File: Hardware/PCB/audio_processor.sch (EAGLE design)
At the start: 33 parts, among them IC1 ADS7042DCU, IC2 ADS7042DCU, J1 TMS-101-51-G-D, J10 TMS-101-51-G-D, J11 MTMM-101-X-X-S-X, J12 TMS-101-51-G-D, J2 MTMM-101-X-X-S-X, J3 TMS-101-51-G-D, J4 MTMM-101-X-X-S-X, J5 MTMM-101-X-X-S-X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

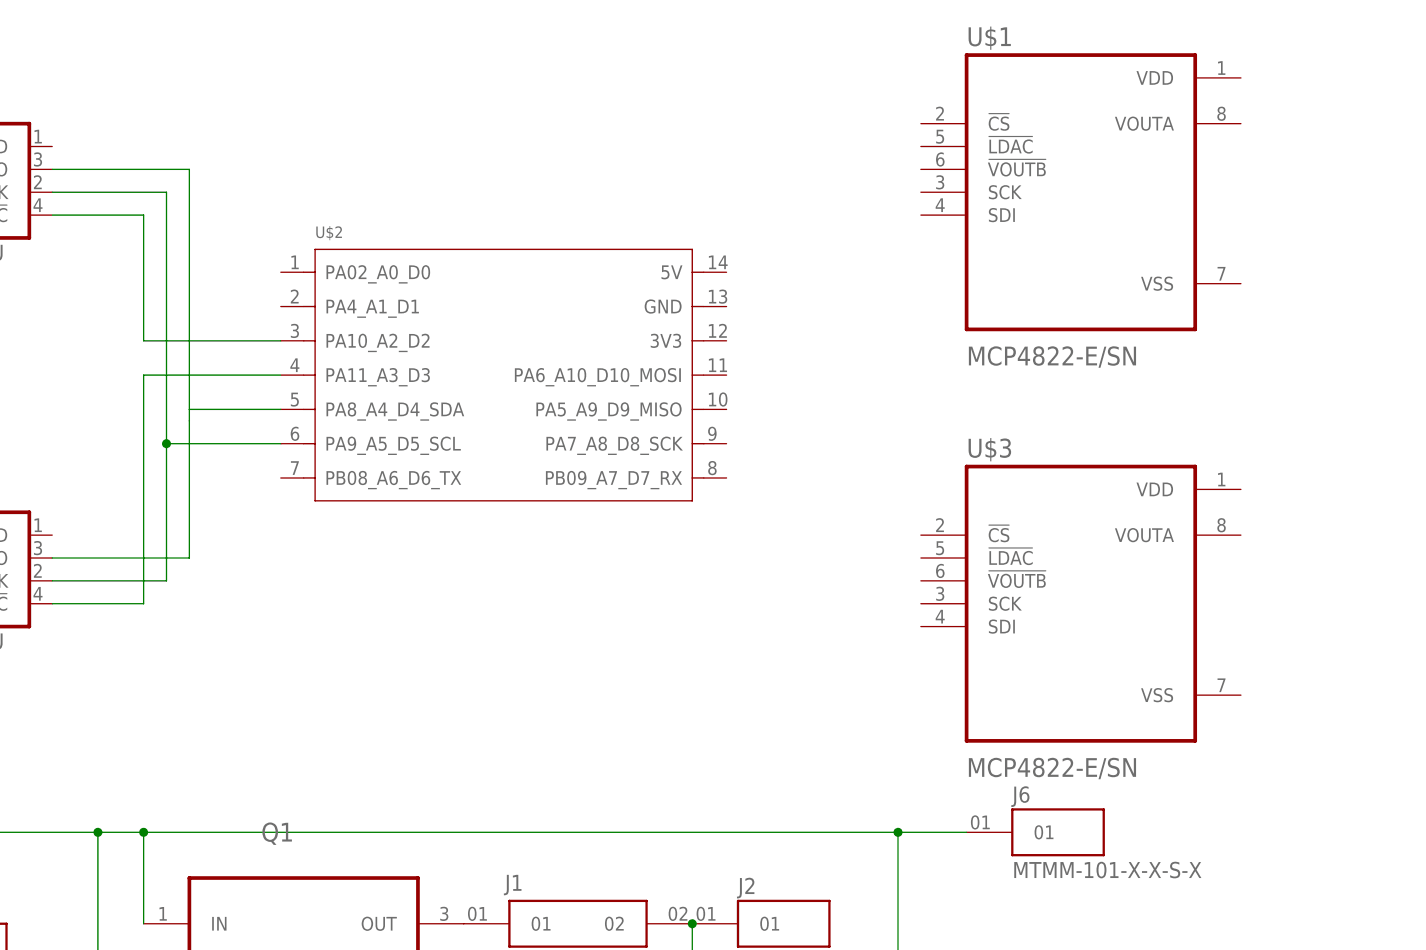
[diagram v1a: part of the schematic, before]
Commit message: AP_0_02
More README detail.
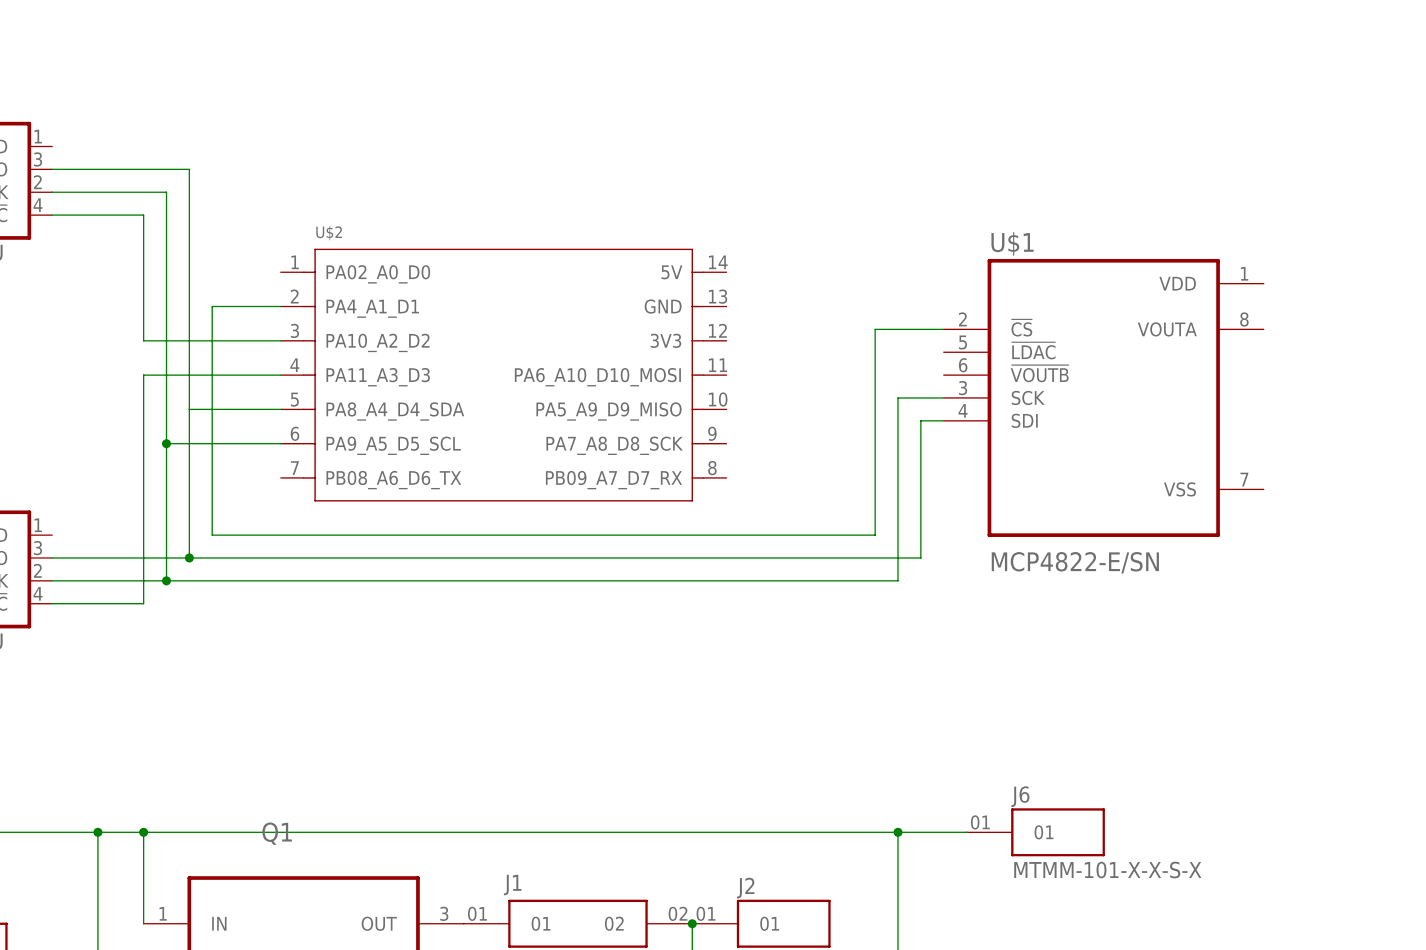
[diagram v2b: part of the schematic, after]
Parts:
- removed U$3: MCP4822-E/SN, MCP4822-E_SN:MCP4822-E/SN
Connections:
- new net N$28: U$1.!CS, U$2.PA4_A1_D1
- net N$21: now also U$1.SCK
- net N$24: now also U$1.SDI
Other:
- moved on the sheet: U$1
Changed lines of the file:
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@@
 </part>
 <part name="IC2" library="Texas Instruments" deviceset="ADS7042" device="DCU" package3d_urn="urn:adsk.eagle:package:7566972/2"/>
-<part name="U$3" library="MCP4822-E_SN" deviceset="MCP4822-E/SN" device=""/>
 </parts>
 <sheets>
@@
 <attribute name="VALUE" x="119.38" y="134.62" size="1.778" layer="96"/>
 </instance>
-<instance part="U$1" gate="A" x="254" y="185.42" smashed="yes">
-<attribute name="NAME" x="241.3" y="201.66" size="2.0828" layer="95" ratio="10" rot="SR0"/>
-<attribute name="VALUE" x="241.3" y="166.18" size="2.0828" layer="96" ratio="10" rot="SR0"/>
+<instance part="U$1" gate="A" x="256.54" y="162.56" smashed="yes">
+<attribute name="NAME" x="243.84" y="178.8" size="2.0828" layer="95" ratio="10" rot="SR0"/>
+<attribute name="VALUE" x="243.84" y="143.32" size="2.0828" layer="96" ratio="10" rot="SR0"/>
 </instance>
 <instance part="U$2" gate="G$1" x="190.5" y="165.1" smashed="yes">
@@
 <attribute name="NAME" x="119.38" y="194.31" size="1.778" layer="95"/>
 <attribute name="VALUE" x="119.38" y="177.8" size="1.778" layer="96"/>
-</instance>
-<instance part="U$3" gate="A" x="254" y="139.7" smashed="yes">
-<attribute name="NAME" x="241.3" y="155.94" size="2.0828" layer="95" ratio="10" rot="SR0"/>
-<attribute name="VALUE" x="241.3" y="120.46" size="2.0828" layer="96" ratio="10" rot="SR0"/>
 </instance>
 </instances>
@@
 <wire x1="165.1" y1="157.48" x2="152.4" y2="157.48" width="0.1524" layer="91"/>
 <junction x="152.4" y="157.48"/>
+<pinref part="U$1" gate="A" pin="SCK"/>
+<wire x1="238.76" y1="162.56" x2="233.68" y2="162.56" width="0.1524" layer="91"/>
+<wire x1="233.68" y1="162.56" x2="233.68" y2="142.24" width="0.1524" layer="91"/>
+<wire x1="233.68" y1="142.24" x2="152.4" y2="142.24" width="0.1524" layer="91"/>
+<junction x="152.4" y="142.24"/>
 </segment>
 </net>
@@
 <wire x1="154.94" y1="187.96" x2="154.94" y2="161.29" width="0.1524" layer="91"/>
 <pinref part="IC1" gate="G$1" pin="SDO"/>
-<wire x1="154.94" y1="160.02" x2="154.94" y2="144.78" width="0.1524" layer="91"/>
+<wire x1="154.94" y1="161.29" x2="154.94" y2="144.78" width="0.1524" layer="91"/>
 <wire x1="154.94" y1="144.78" x2="139.7" y2="144.78" width="0.1524" layer="91"/>
 <pinref part="U$2" gate="G$1" pin="PA8_A4_D4_SDA"/>
 <wire x1="165.1" y1="161.29" x2="154.94" y2="161.29" width="0.1524" layer="91"/>
-<wire x1="154.94" y1="161.29" x2="154.94" y2="160.02" width="0.1524" layer="91"/>
+<pinref part="U$1" gate="A" pin="SDI"/>
+<wire x1="238.76" y1="160.02" x2="236.22" y2="160.02" width="0.1524" layer="91"/>
+<wire x1="236.22" y1="160.02" x2="236.22" y2="144.78" width="0.1524" layer="91"/>
+<wire x1="236.22" y1="144.78" x2="154.94" y2="144.78" width="0.1524" layer="91"/>
+<junction x="154.94" y="144.78"/>
 </segment>
 </net>
@@
 </segment>
 </net>
+<net name="N$28" class="0">
+<segment>
+<pinref part="U$1" gate="A" pin="!CS"/>
+<wire x1="238.76" y1="170.18" x2="231.14" y2="170.18" width="0.1524" layer="91"/>
+<wire x1="231.14" y1="170.18" x2="231.14" y2="147.32" width="0.1524" layer="91"/>
+<wire x1="231.14" y1="147.32" x2="157.48" y2="147.32" width="0.1524" layer="91"/>
+<wire x1="157.48" y1="147.32" x2="157.48" y2="172.72" width="0.1524" layer="91"/>
+<pinref part="U$2" gate="G$1" pin="PA4_A1_D1"/>
+<wire x1="157.48" y1="172.72" x2="165.1" y2="172.72" width="0.1524" layer="91"/>
+</segment>
+</net>

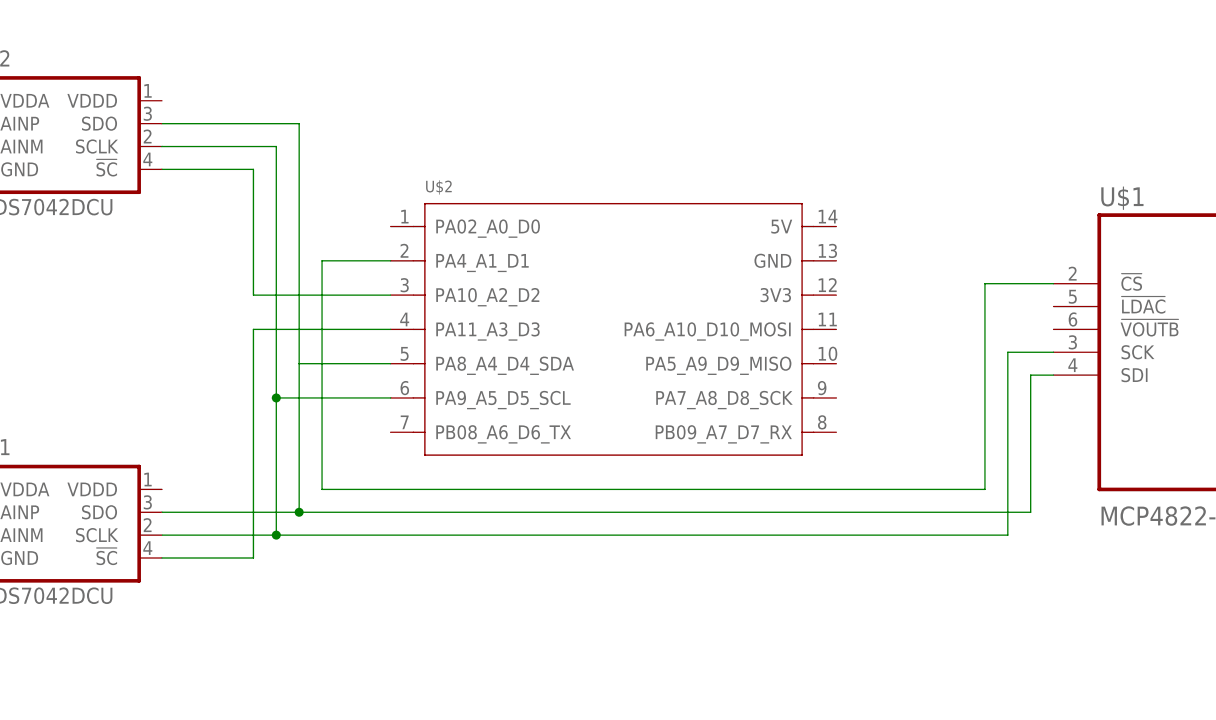
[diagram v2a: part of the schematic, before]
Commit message: AP_0_03
First public commit.  Uses timer group (as opposed to GPTimer).
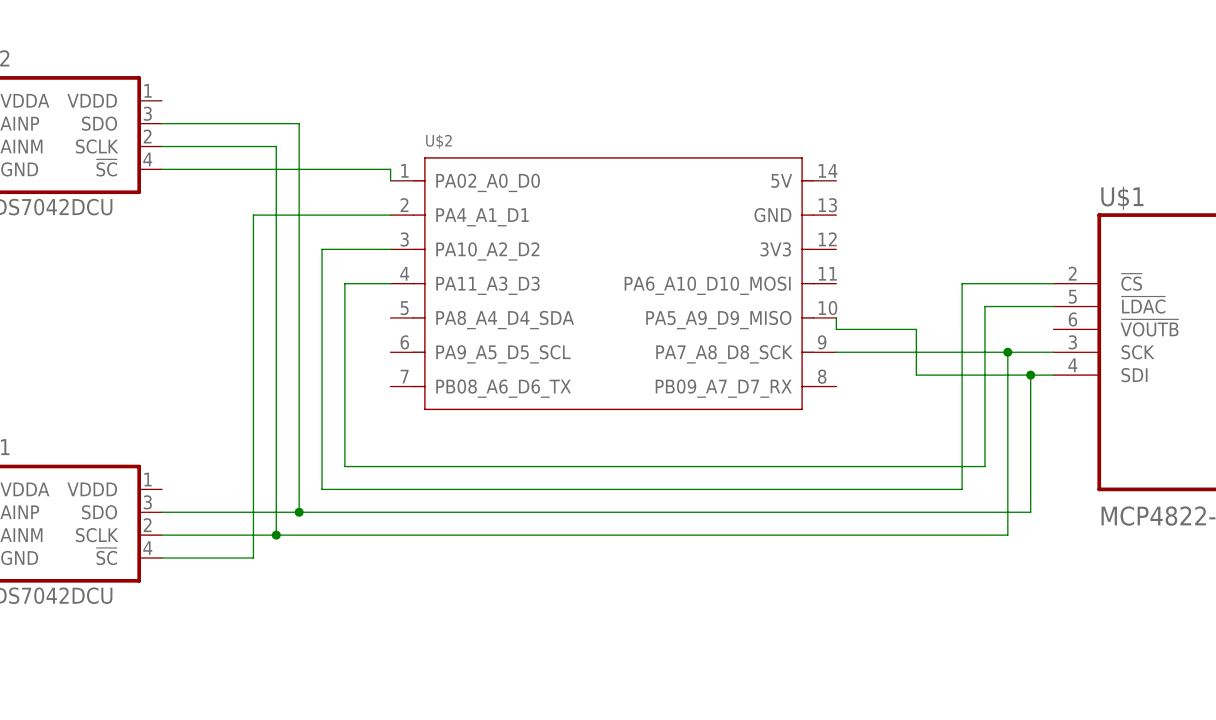
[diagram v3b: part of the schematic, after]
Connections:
- new net N$20: U$1.!LDAC, U$2.PA11_A3_D3
- net N$21: now also U$2.PA7_A8_D8_SCK; no longer U$2.PA9_A5_D5_SCL
- net N$24: now also U$2.PA5_A9_D9_MISO; no longer U$2.PA8_A4_D4_SDA
- net N$25: now also U$2.PA4_A1_D1; no longer U$2.PA11_A3_D3
- net N$26: now also U$2.PA02_A0_D0; no longer U$2.PA10_A2_D2
- net N$28: now also U$2.PA10_A2_D2; no longer U$2.PA4_A1_D1
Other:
- moved on the sheet: U$2
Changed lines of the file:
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@@
 <attribute name="VALUE" x="243.84" y="143.32" size="2.0828" layer="96" ratio="10" rot="SR0"/>
 </instance>
-<instance part="U$2" gate="G$1" x="190.5" y="165.1" smashed="yes">
-<attribute name="NAME" x="168.91" y="180.34" size="1.27" layer="95" ratio="12"/>
-<attribute name="VALUE" x="168.91" y="179.07" size="1.27" layer="96" ratio="12"/>
+<instance part="U$2" gate="G$1" x="190.5" y="170.18" smashed="yes">
+<attribute name="NAME" x="168.91" y="185.42" size="1.27" layer="95" ratio="12"/>
+<attribute name="VALUE" x="168.91" y="184.15" size="1.27" layer="96" ratio="12"/>
 </instance>
 <instance part="U2" gate="A" x="88.9" y="182.88" smashed="yes">
@@
 <pinref part="IC2" gate="G$1" pin="SCLK"/>
 <wire x1="139.7" y1="185.42" x2="152.4" y2="185.42" width="0.1524" layer="91"/>
-<wire x1="152.4" y1="185.42" x2="152.4" y2="157.48" width="0.1524" layer="91"/>
-<wire x1="152.4" y1="157.48" x2="152.4" y2="142.24" width="0.1524" layer="91"/>
+<wire x1="152.4" y1="185.42" x2="152.4" y2="142.24" width="0.1524" layer="91"/>
 <wire x1="152.4" y1="142.24" x2="139.7" y2="142.24" width="0.1524" layer="91"/>
-<pinref part="U$2" gate="G$1" pin="PA9_A5_D5_SCL"/>
-<wire x1="165.1" y1="157.48" x2="152.4" y2="157.48" width="0.1524" layer="91"/>
-<junction x="152.4" y="157.48"/>
 <pinref part="U$1" gate="A" pin="SCK"/>
 <wire x1="238.76" y1="162.56" x2="233.68" y2="162.56" width="0.1524" layer="91"/>
@@
 <wire x1="233.68" y1="142.24" x2="152.4" y2="142.24" width="0.1524" layer="91"/>
 <junction x="152.4" y="142.24"/>
+<pinref part="U$2" gate="G$1" pin="PA7_A8_D8_SCK"/>
+<wire x1="214.63" y1="162.56" x2="233.68" y2="162.56" width="0.1524" layer="91"/>
+<junction x="233.68" y="162.56"/>
 </segment>
 </net>
@@
 <pinref part="IC2" gate="G$1" pin="SDO"/>
 <wire x1="139.7" y1="187.96" x2="154.94" y2="187.96" width="0.1524" layer="91"/>
-<wire x1="154.94" y1="187.96" x2="154.94" y2="161.29" width="0.1524" layer="91"/>
 <pinref part="IC1" gate="G$1" pin="SDO"/>
-<wire x1="154.94" y1="161.29" x2="154.94" y2="144.78" width="0.1524" layer="91"/>
+<wire x1="154.94" y1="187.96" x2="154.94" y2="144.78" width="0.1524" layer="91"/>
 <wire x1="154.94" y1="144.78" x2="139.7" y2="144.78" width="0.1524" layer="91"/>
-<pinref part="U$2" gate="G$1" pin="PA8_A4_D4_SDA"/>
-<wire x1="165.1" y1="161.29" x2="154.94" y2="161.29" width="0.1524" layer="91"/>
 <pinref part="U$1" gate="A" pin="SDI"/>
 <wire x1="238.76" y1="160.02" x2="236.22" y2="160.02" width="0.1524" layer="91"/>
@@
 <wire x1="236.22" y1="144.78" x2="154.94" y2="144.78" width="0.1524" layer="91"/>
 <junction x="154.94" y="144.78"/>
+<wire x1="236.22" y1="160.02" x2="223.52" y2="160.02" width="0.1524" layer="91"/>
+<junction x="236.22" y="160.02"/>
+<wire x1="223.52" y1="160.02" x2="223.52" y2="165.1" width="0.1524" layer="91"/>
+<pinref part="U$2" gate="G$1" pin="PA5_A9_D9_MISO"/>
+<wire x1="223.52" y1="165.1" x2="214.63" y2="165.1" width="0.1524" layer="91"/>
+<wire x1="214.63" y1="165.1" x2="214.63" y2="166.37" width="0.1524" layer="91"/>
 </segment>
 </net>
@@
 <pinref part="IC1" gate="G$1" pin="!SC"/>
 <wire x1="139.7" y1="139.7" x2="149.86" y2="139.7" width="0.1524" layer="91"/>
+<wire x1="149.86" y1="139.7" x2="149.86" y2="177.8" width="0.1524" layer="91"/>
+<pinref part="U$2" gate="G$1" pin="PA4_A1_D1"/>
+<wire x1="165.1" y1="177.8" x2="149.86" y2="177.8" width="0.1524" layer="91"/>
+</segment>
+</net>
+<net name="N$26" class="0">
+<segment>
+<pinref part="IC2" gate="G$1" pin="!SC"/>
+<pinref part="U$2" gate="G$1" pin="PA02_A0_D0"/>
+<wire x1="139.7" y1="182.88" x2="165.1" y2="182.88" width="0.1524" layer="91"/>
+<wire x1="165.1" y1="182.88" x2="165.1" y2="181.61" width="0.1524" layer="91"/>
+</segment>
+</net>
+<net name="N$28" class="0">
+<segment>
+<pinref part="U$1" gate="A" pin="!CS"/>
+<wire x1="238.76" y1="170.18" x2="228.6" y2="170.18" width="0.1524" layer="91"/>
+<wire x1="228.6" y1="170.18" x2="228.6" y2="147.32" width="0.1524" layer="91"/>
+<wire x1="228.6" y1="147.32" x2="157.48" y2="147.32" width="0.1524" layer="91"/>
+<pinref part="U$2" gate="G$1" pin="PA10_A2_D2"/>
+<wire x1="165.1" y1="173.99" x2="157.48" y2="173.99" width="0.1524" layer="91"/>
+<wire x1="157.48" y1="173.99" x2="157.48" y2="147.32" width="0.1524" layer="91"/>
+</segment>
+</net>
+<net name="N$20" class="0">
+<segment>
+<pinref part="U$1" gate="A" pin="!LDAC"/>
+<wire x1="238.76" y1="167.64" x2="231.14" y2="167.64" width="0.1524" layer="91"/>
+<wire x1="231.14" y1="167.64" x2="231.14" y2="149.86" width="0.1524" layer="91"/>
+<wire x1="231.14" y1="149.86" x2="160.02" y2="149.86" width="0.1524" layer="91"/>
 <pinref part="U$2" gate="G$1" pin="PA11_A3_D3"/>
-<wire x1="149.86" y1="139.7" x2="149.86" y2="165.1" width="0.1524" layer="91"/>
-<wire x1="149.86" y1="165.1" x2="165.1" y2="165.1" width="0.1524" layer="91"/>
-</segment>
-</net>
-<net name="N$26" class="0">
-<segment>
-<pinref part="IC2" gate="G$1" pin="!SC"/>
-<wire x1="139.7" y1="182.88" x2="149.86" y2="182.88" width="0.1524" layer="91"/>
-<pinref part="U$2" gate="G$1" pin="PA10_A2_D2"/>
-<wire x1="149.86" y1="182.88" x2="149.86" y2="168.91" width="0.1524" layer="91"/>
-<wire x1="149.86" y1="168.91" x2="165.1" y2="168.91" width="0.1524" layer="91"/>
-</segment>
-</net>
-<net name="N$28" class="0">
-<segment>
-<pinref part="U$1" gate="A" pin="!CS"/>
-<wire x1="238.76" y1="170.18" x2="231.14" y2="170.18" width="0.1524" layer="91"/>
-<wire x1="231.14" y1="170.18" x2="231.14" y2="147.32" width="0.1524" layer="91"/>
-<wire x1="231.14" y1="147.32" x2="157.48" y2="147.32" width="0.1524" layer="91"/>
-<wire x1="157.48" y1="147.32" x2="157.48" y2="172.72" width="0.1524" layer="91"/>
-<pinref part="U$2" gate="G$1" pin="PA4_A1_D1"/>
-<wire x1="157.48" y1="172.72" x2="165.1" y2="172.72" width="0.1524" layer="91"/>
-</segment>
-</net>
+<wire x1="165.1" y1="170.18" x2="160.02" y2="170.18" width="0.1524" layer="91"/>
+<wire x1="160.02" y1="170.18" x2="160.02" y2="149.86" width="0.1524" layer="91"/>
+</segment>
+</net>

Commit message: AP_0_05
Updated README.
Barrel connector library added.
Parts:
- added J9: PJ-102AH, PJ-102AH:PJ-102AH
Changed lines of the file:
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@@
 </part>
 <part name="IC2" library="Texas Instruments" deviceset="ADS7042" device="DCU" package3d_urn="urn:adsk.eagle:package:7566972/2"/>
+<part name="J9" library="PJ-102AH" deviceset="PJ-102AH" device=""/>
 </parts>
 <sheets>
@@
 <attribute name="VALUE" x="119.38" y="177.8" size="1.778" layer="96"/>
 </instance>
+<instance part="J9" gate="G$1" x="25.4" y="185.42" smashed="yes">
+<attribute name="NAME" x="17.774240625" y="190.503840625" size="1.779340625" layer="95"/>
+<attribute name="VALUE" x="17.77045" y="180.33363125" size="1.78023125" layer="96"/>
+</instance>
 </instances>
